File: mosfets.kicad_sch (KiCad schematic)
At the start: 32 parts, among them Q10 IXTP90N15T, Q11 IXTP90N15T, Q12 IXTP90N15T, Q13 IXTP90N15T, U10 IRS21867S, U6 IRS21867S, U7 IR2110, U9 IRS21867S

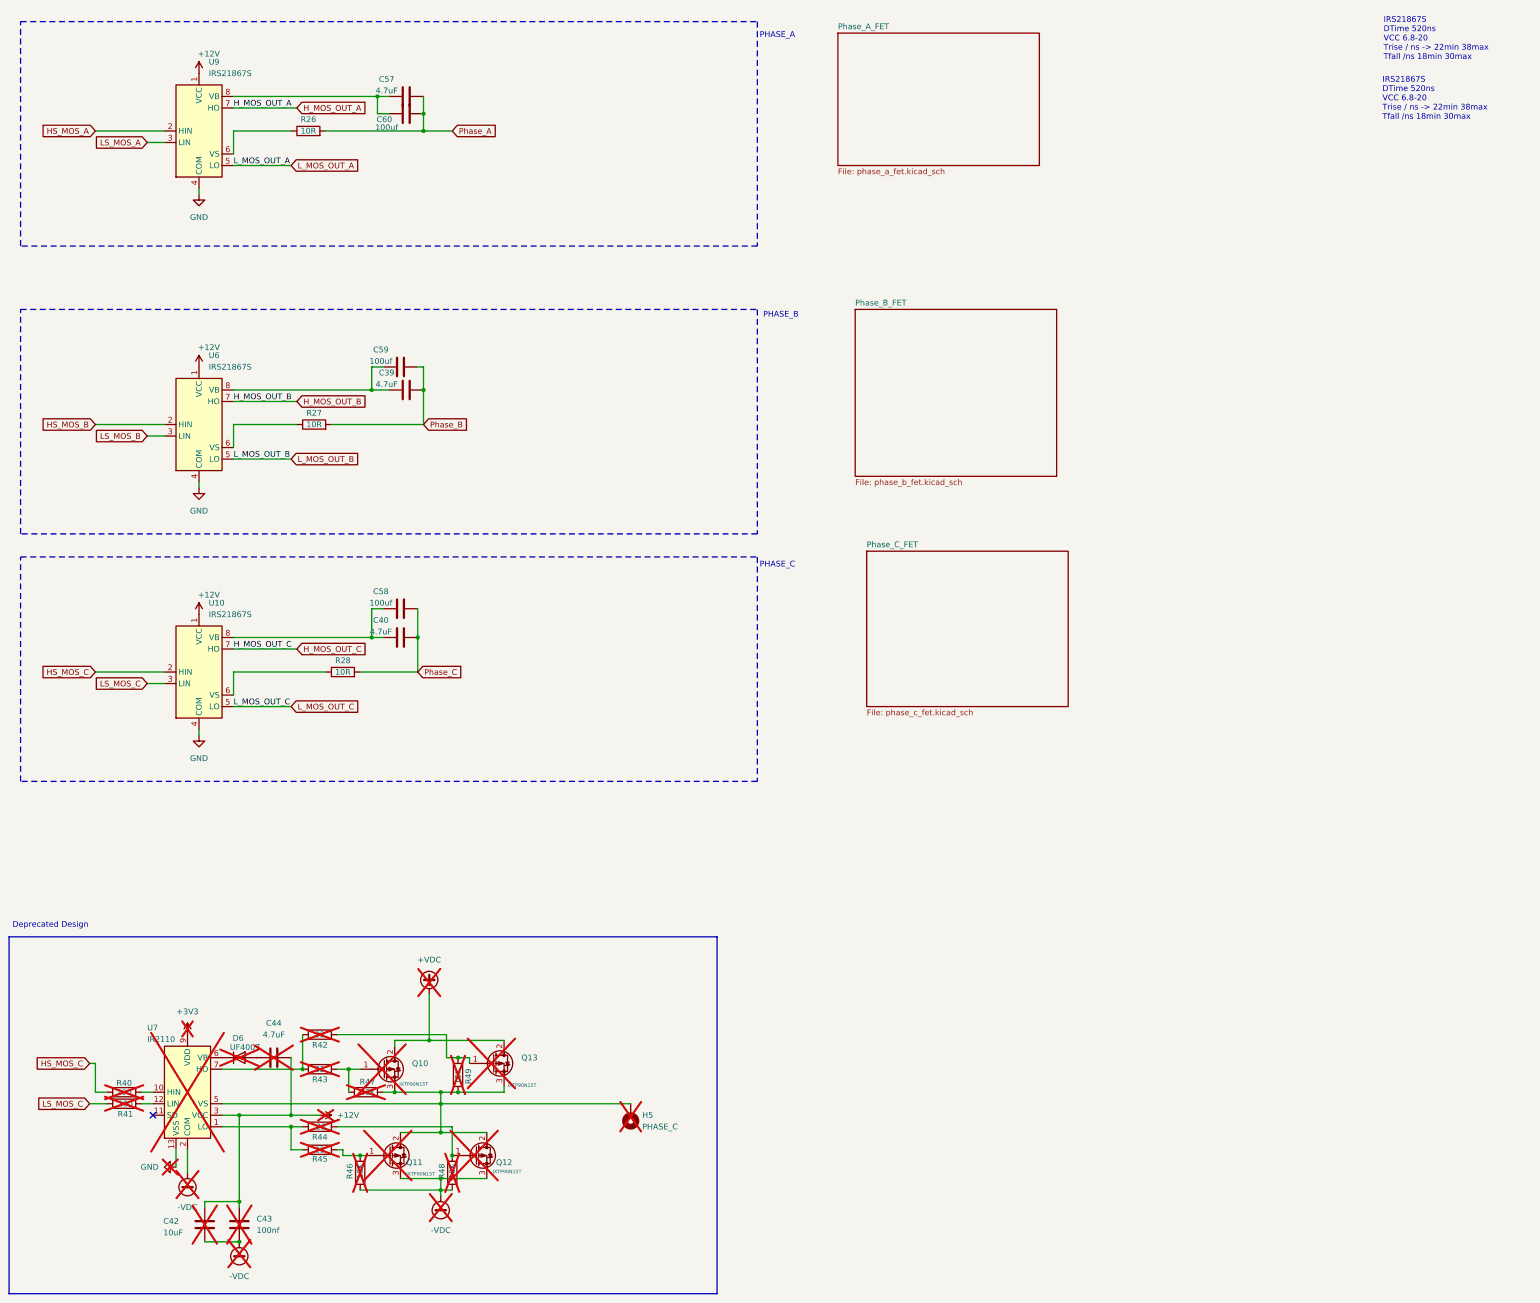
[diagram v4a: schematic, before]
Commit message: update: revised label
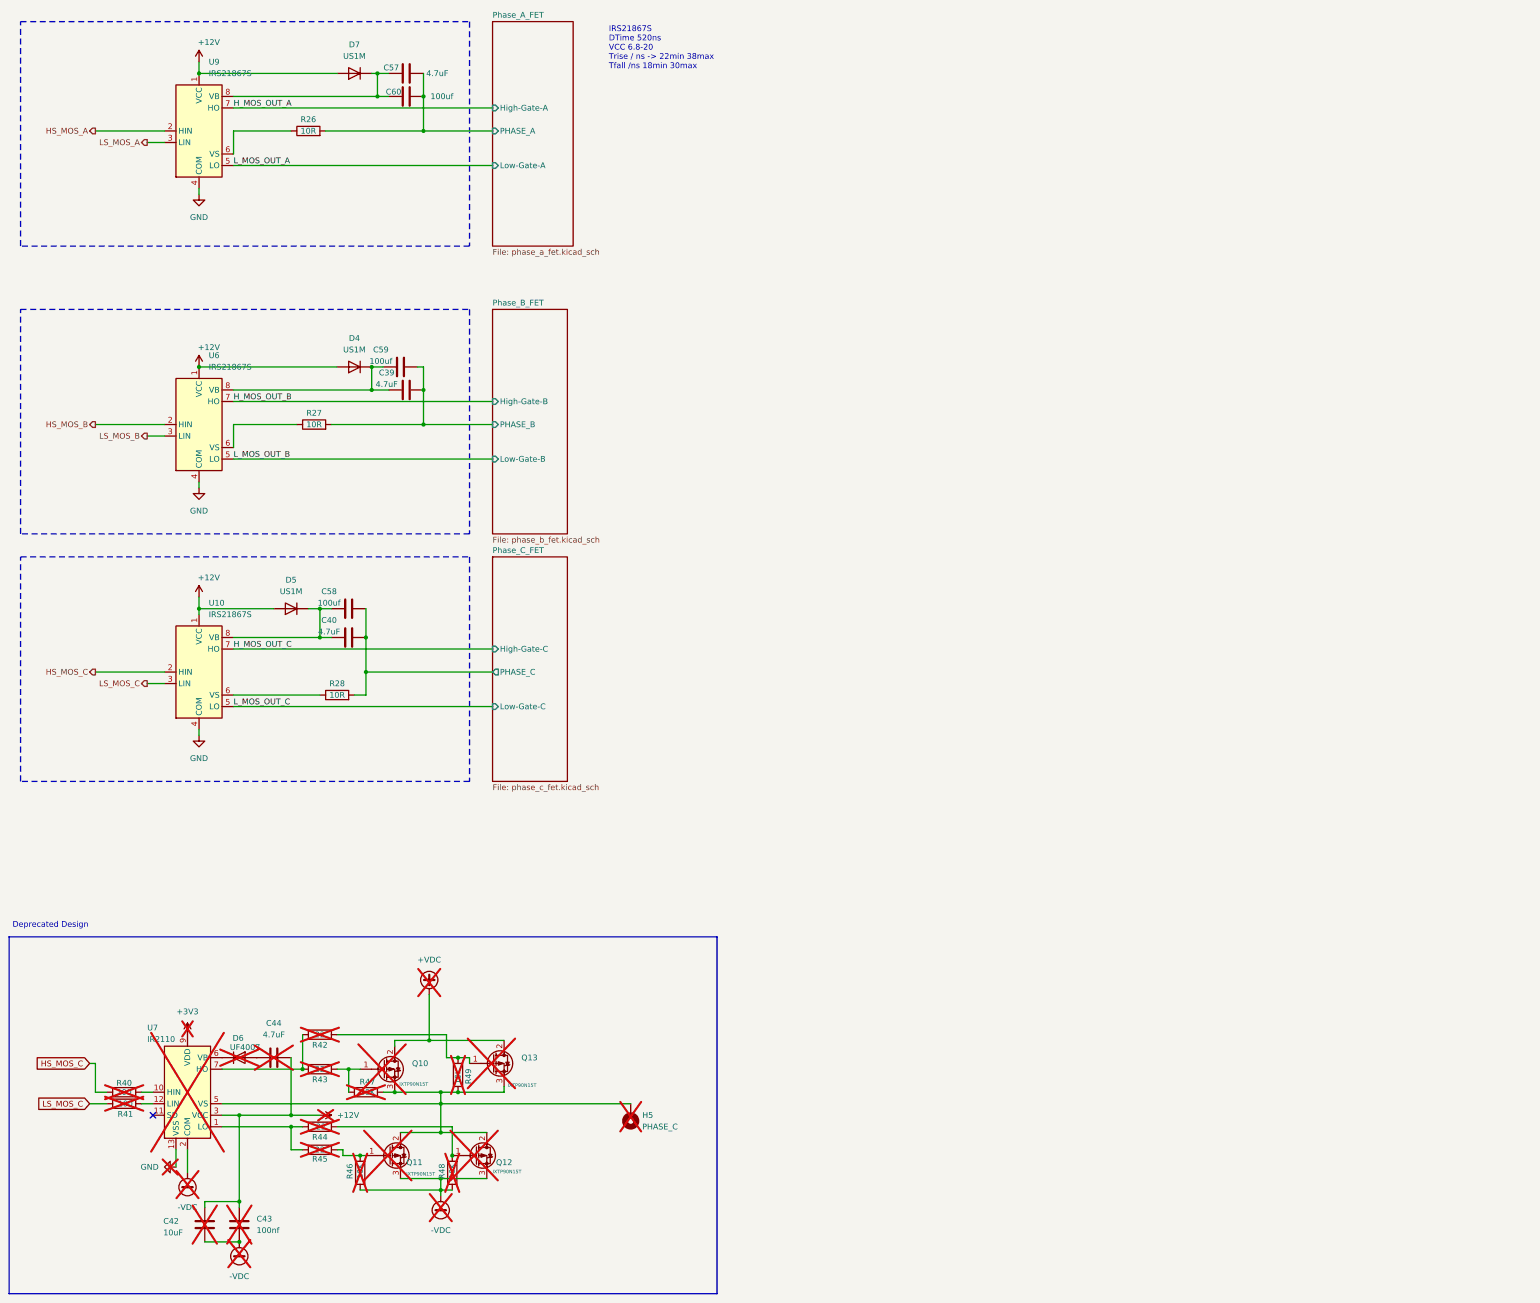
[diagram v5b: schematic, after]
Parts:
- added D4, D5, D7: US1M, Diode_SMD:D_SMA, symbol Diode:US1M
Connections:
- net +12V: now also D4.2 (A), D5.2 (A), D7.2 (A)
- net at C40.1, C58.1, U10.8 (VB): now also D5.1 (K)
- net at C57.1, C60.1, U9.8 (VB): now also D7.1 (K)
- net at C39.1, C59.1, U6.8 (VB): now also D4.1 (K)
- net Phase_A renamed Phase_A_FET/PHASE_A
- net Phase_B renamed Phase_B_FET/PHASE_B
- net Phase_C renamed Phase_C_FET/PHASE_C
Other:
- sheet Phase_A_FET ports: added High-Gate-A, Low-Gate-A, PHASE_A; removed none
- sheet Phase_B_FET ports: added High-Gate-B, Low-Gate-B, PHASE_B; removed none
- sheet Phase_C_FET ports: added High-Gate-C, Low-Gate-C, PHASE_C; removed none
- note removed: "PHASE_A"
- note removed: "PHASE_B"
- note removed: "PHASE_C"
- moved on the sheet: C40, C57, C58, C60, R28
